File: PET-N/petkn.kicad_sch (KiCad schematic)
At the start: 83 parts, among them J1 Conn_01x20, J2 Conn_02x03_Odd_Even, J3 LINK3, J4 Conn_01x20, J5 SPACE1, J6 SPACE2, J67 LINK67, SW1 KP "=", SW10 KP "0", SW11 R SHIFT, SW12 ">", SW14 "]", SW15 "@", SW16 L SHIFT, SW17 KP "+", SW18 KP "2", SW2 KP ".", SW20 "?", SW21 ",", SW22 "N", SW23 "V", SW24 "X", SW25 KP "3", SW26 KP "1", SW27 RETURN, SW28 ";", SW29 "M", SW3 NC ($10), SW30 "B", SW31 "C", SW32 "Z", SW320 S LOCK, SW33 KP "*", SW34 KP "5", SW36 ":", SW37 "K", SW38 "H", SW39 "F", SW4 STOP, SW40 "S", SW41 KP "6", SW42 KP "4", SW44 "L", SW45 "J", SW46 "G", SW47 "D", SW48 "A", SW49 KP "/", SW5 "<", SW50 KP "8", SW52 "P", SW53 "I", SW54 "Y", SW55 "R", SW56 "W", SW57 KP "9", SW58 KP "7", SW59 U ARROW, SW6 SPACE, SW60 "O", SW61 "U", SW62 "T", SW63 "E", SW64 "Q", SW65 INS/DEL, SW66 UP/DOWN, SW67 NC ($0A), SW68 ")", SW69 "\", SW7 "[", SW70 "'", SW71 "$", SW72 QUOTE, SW73 LEFT/RIGHT, SW74 CLR/HOME, SW75 B ARROW, SW76 "(", SW77 "&", SW78 "%", SW79 "#"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

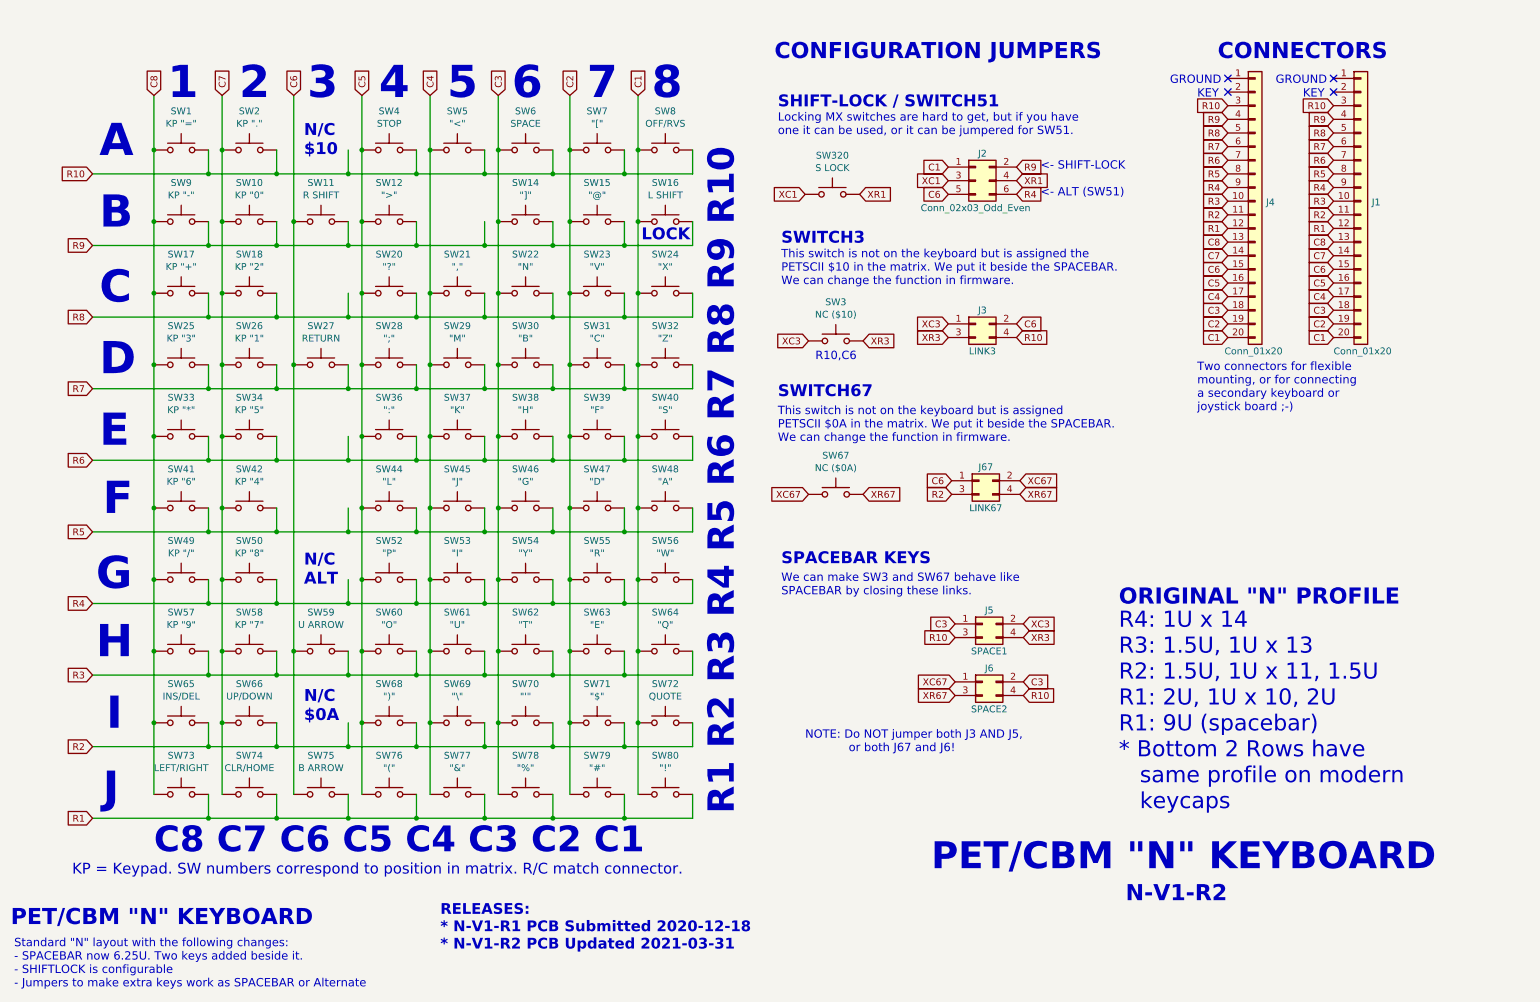
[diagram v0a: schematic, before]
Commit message: first work on adding LEDs and extended connector
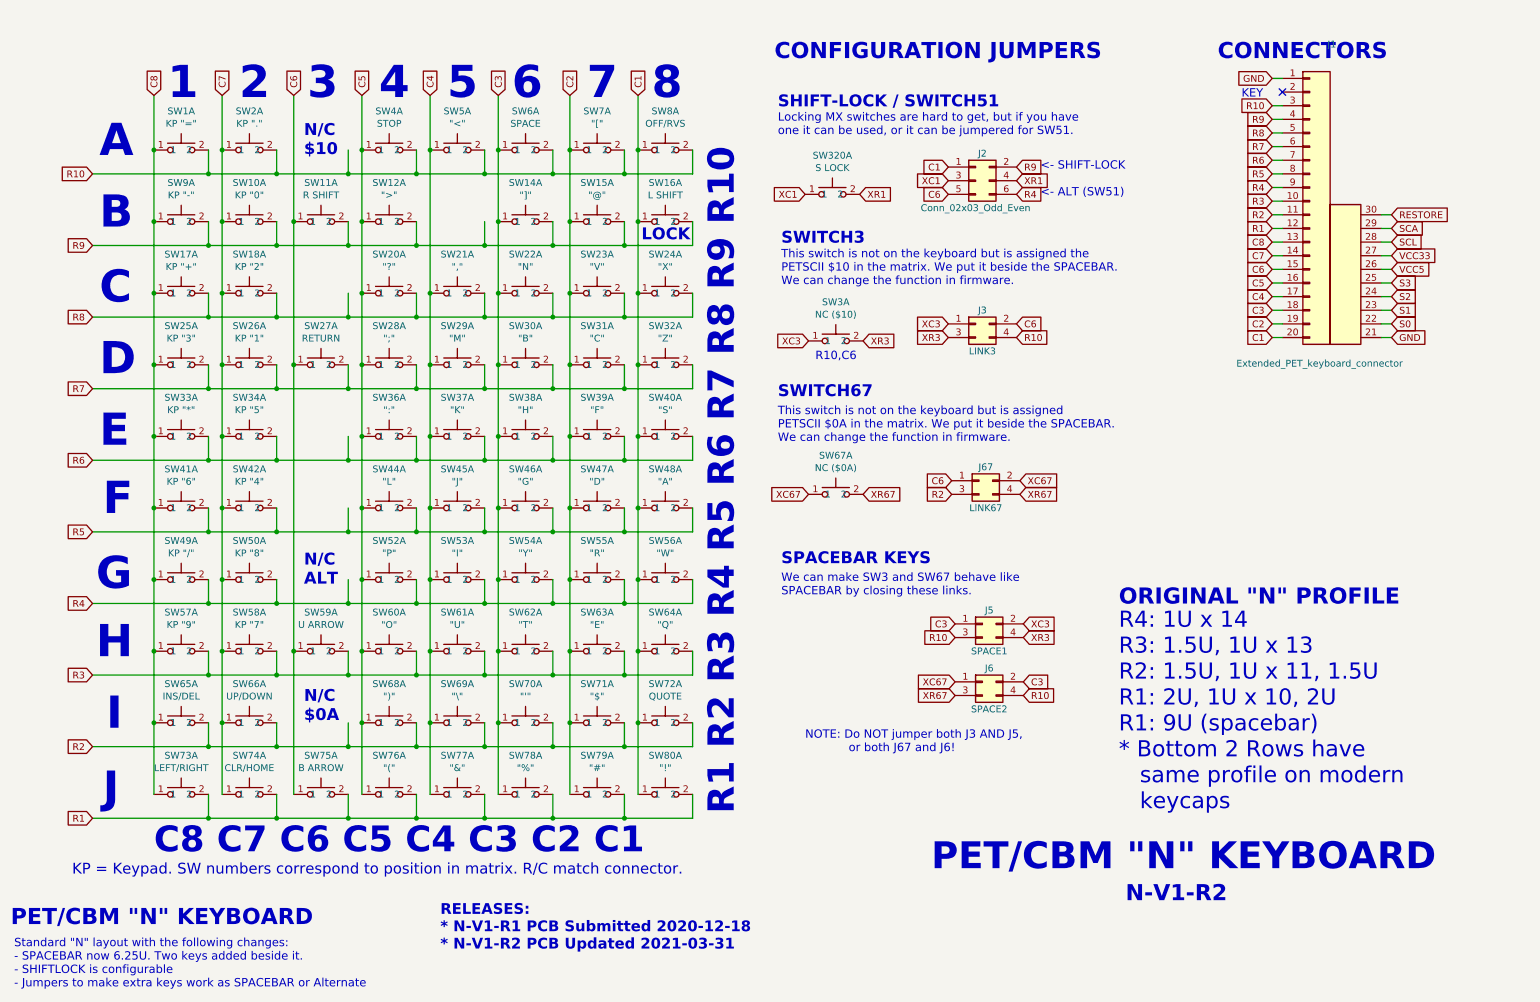
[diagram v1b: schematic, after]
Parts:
- removed J1, J4: Conn_01x20, Connector_PinHeader_2.54mm:PinHeader_1x20_P2.54mm_Vertical, symbol Connector_Generic:Conn_01x20
- added J1: Extended_PET_keyboard_connector, petkn:PET_Extended_Keyboard_Connector, symbol petkn:Extended_PET_keyboard_connector
- SW1, SW10, SW12, SW14, SW15, SW17, SW18, SW2, SW20, SW21, SW22, SW23, SW24, SW25, SW26, SW28, SW29, SW30, SW31, SW32, SW33, SW34, SW36, SW37, SW38, SW39, SW4, SW40, SW41, SW42, SW44, SW45, SW46, SW47, SW48, SW49, SW5, SW50, SW52, SW53, SW54, SW55, SW56, SW57, SW58, SW59, SW60, SW61, SW62, SW63, SW64, SW65, SW66, SW68, SW69, SW7, SW70, SW71, SW72, SW73, SW74, SW75, SW76, SW77, SW78, SW79, SW80, SW9: footprint Button_Switch_Keyboard:SW_Cherry_MX_1.00u_PCB -> petkn:SW_Cherry_MX_1.00u_PCB_with_LED; symbol Switch:SW_Push -> petkn:MX Key with LED Unit
- SW11, SW16: footprint Button_Switch_Keyboard:SW_Cherry_MX_2.00u_PCB -> petkn:SW_Cherry_MX_2.00u_PCB_with_LED; symbol Switch:SW_Push -> petkn:MX Key with LED Unit
- SW27, SW320, SW8: footprint Button_Switch_Keyboard:SW_Cherry_MX1A_1.50u_PCB -> petkn:SW_Cherry_MX_1.50u_PCB_with_LED; symbol Switch:SW_Push -> petkn:MX Key with LED Unit
- SW3: footprint Button_Switch_Keyboard:SW_Cherry_MX1A_1.25u_PCB -> petkn:SW_Cherry_MX_1.25u_PCB_with_LED; symbol Switch:SW_Push -> petkn:MX Key with LED Unit
- SW6: footprint Button_Switch_Keyboard:SW_Cherry_MX1A_6.25u_PCB -> petkn:SW_Cherry_MX_6.25u_PCB_with_LED; symbol Switch:SW_Push -> petkn:MX Key with LED Unit
- SW67: footprint Button_Switch_Keyboard:SW_Cherry_MX_1.50u_PCB -> petkn:SW_Cherry_MX_1.50u_PCB_with_LED; symbol Switch:SW_Push -> petkn:MX Key with LED Unit
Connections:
- net C1: now also J1.20 (C1)
- net C2: now also J1.19 (C2)
- net C3: now also J1.18 (C3)
- net C4: now also J1.17 (C4)
- net C5: now also J1.16 (C5)
- net C6: now also J1.15 (C6)
- net C7: now also J1.14 (C7)
- net C8: now also J1.13 (C8)
- net R1: now also J1.12 (R1)
- net R10: now also J1.3 (R10)
- net R2: now also J1.11 (R2)
- net R3: now also J1.10 (R3)
- net R4: now also J1.9 (R4)
- net R5: now also J1.8 (R5)
- net R6: now also J1.7 (R6)
- net R7: now also J1.6 (R7)
- net R8: now also J1.5 (R8)
- net R9: now also J1.4 (R9)
- new net GND: J1.1 (GND), J1.21 (GND)
- new net RESTORE: J1.30 (RESTORE)
- new net S0: J1.22 (S0)
- new net S1: J1.23 (S1)
- new net S2: J1.24 (S2)
- new net S3: J1.25 (S3)
- new net SCA: J1.29 (SCA)
- new net SCL: J1.28 (SCL)
- new net VCC33: J1.27 (VCC33)
- new net VCC5: J1.26 (VCC5)
- no-connect marks 4 -> 1
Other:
- note removed: "GROUND"
- note removed: "Two connectors for flexible mounting, or for connecting a secondary keyboard or joystick board ;-)"

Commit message: add extension page, add 4-to-10 decoder
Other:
- added sheet Extensions (extensions.kicad_sch)

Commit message: work on R3 of keyboard pcb
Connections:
- net VCC5 renamed VCC
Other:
- added sheet Driver (driver.kicad_sch)
- added sheet Row decoder (decoder.kicad_sch)
- added sheet i2c (i2c.kicad_sch)
- added sheet stick (stick.kicad_sch)
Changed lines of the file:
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@@
 		)
 	)
-	(global_label "VCC5"
+	(global_label "VCC"
 		(shape input)
 		(at 271.78 62.23 0)
@@
 		)
 		(property "Intersheetrefs" "${INTERSHEET_REFS}"
-			(at 278.9491 62.23 0)
+			(at 277.7396 62.23 0)
 			(effects
 				(font
@@
 	)
 	(sheet
+		(at 244.475 88.265)
+		(size 12.7 3.81)
+		(exclude_from_sim no)
+		(in_bom yes)
+		(on_board yes)
+		(dnp no)
+		(fields_autoplaced yes)
+		(stroke
+			(width 0.1524)
+			(type solid)
+		)
+		(fill
+			(color 0 0 0 0.0000)
+		)
+		(property "Sheetname" "i2c"
+			(at 244.475 87.5534 0)
+			(effects
+				(font
+					(size 1.27 1.27)
+				)
+				(justify left bottom)
+			)
+		)
+		(property "Sheetfile" "i2c.kicad_sch"
+			(at 244.475 92.6596 0)
+			(effects
+				(font
+					(size 1.27 1.27)
+				)
+				(justify left top)
+			)
+		)
+		(instances
+			(project "petkn"
+				(path "/a0727808-af70-4056-b2ee-ab828c2acfbd"
+					(page "3")
+				)
+			)
+		)
+	)
+	(sheet
+		(at 220.345 104.14)
+		(size 12.7 3.81)
+		(exclude_from_sim no)
+		(in_bom yes)
+		(on_board yes)
+		(dnp no)
+		(fields_autoplaced yes)
+		(stroke
+			(width 0.1524)
+			(type solid)
+		)
+		(fill
+			(color 0 0 0 0.0000)
+		)
+		(property "Sheetname" "stick"
+			(at 220.345 103.4284 0)
+			(effects
+				(font
+					(size 1.27 1.27)
+				)
+				(justify left bottom)
+			)
+		)
+		(property "Sheetfile" "stick.kicad_sch"
+			(at 220.345 108.5346 0)
+			(effects
+				(font
+					(size 1.27 1.27)
+				)
+				(justify left top)
+			)
+		)
+		(instances
+			(project "petkn"
+				(path "/a0727808-af70-4056-b2ee-ab828c2acfbd"
+					(page "6")
+				)
+			)
+		)
+	)
+	(sheet
+		(at 269.875 106.045)
+		(size 12.7 3.81)
+		(exclude_from_sim no)
+		(in_bom yes)
+		(on_board yes)
+		(dnp no)
+		(fields_autoplaced yes)
+		(stroke
+			(width 0.1524)
+			(type solid)
+		)
+		(fill
+			(color 0 0 0 0.0000)
+		)
+		(property "Sheetname" "Row decoder"
+			(at 269.875 105.3334 0)
+			(effects
+				(font
+					(size 1.27 1.27)
+				)
+				(justify left bottom)
+			)
+		)
+		(property "Sheetfile" "decoder.kicad_sch"
+			(at 269.875 110.4396 0)
+			(effects
+				(font
+					(size 1.27 1.27)
+				)
+				(justify left top)
+			)
+		)
+		(instances
+			(project "petkn"
+				(path "/a0727808-af70-4056-b2ee-ab828c2acfbd"
+					(page "5")
+				)
+			)
+		)
+	)
+	(sheet
 		(at 242.697 102.108)
 		(size 12.7 8.001)
@@
 				)
 			)
+		)
+	)
+	(sheet
+		(at 267.97 90.805)
+		(size 12.7 3.81)
+		(exclude_from_sim no)
+		(in_bom yes)
+		(on_board yes)
+		(dnp no)
+		(fields_autoplaced yes)
+		(stroke
+			(width 0.1524)
+			(type solid)
+		)
+		(fill
+			(color 0 0 0 0.0000)
+		)
+		(property "Sheetname" "Driver"
+			(at 267.97 90.0934 0)
+			(effects
+				(font
+					(size 1.27 1.27)
+				)
+				(justify left bottom)
+			)
+		)
+		(property "Sheetfile" "driver.kicad_sch"
+			(at 267.97 95.1996 0)
+			(effects
+				(font
+					(size 1.27 1.27)
+				)
+				(justify left top)
+			)
+		)
+		(instances
+			(project "petkn"
+				(path "/a0727808-af70-4056-b2ee-ab828c2acfbd"
+					(page "4")
+				)
+			)

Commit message: PET-N r3
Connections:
- net SCA renamed SDA
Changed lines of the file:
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@@
 		)
 	)
-	(global_label "SCA"
+	(global_label "SDA"
 		(shape input)
 		(at 271.78 54.61 0)

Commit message: new schematics version mainly complete
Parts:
- removed J1: Extended_PET_keyboard_connector, petkn:PET_Extended_Keyboard_Connector, symbol petkn:Extended_PET_keyboard_connector
- removed J2: Conn_02x03_Odd_Even, Connector_PinHeader_2.54mm:PinHeader_2x03_P2.54mm_Vertical, symbol Connector_Generic:Conn_02x03_Odd_Even
- removed J3: LINK3, Connector_PinHeader_2.54mm:PinHeader_2x02_P2.54mm_Vertical, symbol Connector_Generic:Conn_02x02_Odd_Even
- removed J5: SPACE1, Connector_PinHeader_2.54mm:PinHeader_2x02_P2.54mm_Vertical, symbol Connector_Generic:Conn_02x02_Odd_Even
- removed J6: SPACE2, Connector_PinHeader_2.54mm:PinHeader_2x02_P2.54mm_Vertical, symbol Connector_Generic:Conn_02x02_Odd_Even
- removed J67: LINK67, Connector_PinHeader_2.54mm:PinHeader_2x02_P2.54mm_Vertical, symbol Connector_Generic:Conn_02x02_Odd_Even
- removed SW1: KP "=", petkn:SW_Cherry_MX_1.00u_PCB_with_LED, symbol petkn:MX Key with LED Unit
- removed SW10: KP "0", petkn:SW_Cherry_MX_1.00u_PCB_with_LED, symbol petkn:MX Key with LED Unit
- removed SW11: R SHIFT, petkn:SW_Cherry_MX_2.00u_PCB_with_LED, symbol petkn:MX Key with LED Unit
- removed SW12: ">", petkn:SW_Cherry_MX_1.00u_PCB_with_LED, symbol petkn:MX Key with LED Unit
- removed SW14: "]", petkn:SW_Cherry_MX_1.00u_PCB_with_LED, symbol petkn:MX Key with LED Unit
- removed SW15: "@", petkn:SW_Cherry_MX_1.00u_PCB_with_LED, symbol petkn:MX Key with LED Unit
- removed SW16: L SHIFT, petkn:SW_Cherry_MX_2.00u_PCB_with_LED, symbol petkn:MX Key with LED Unit
- removed SW17: KP "+", petkn:SW_Cherry_MX_1.00u_PCB_with_LED, symbol petkn:MX Key with LED Unit
- removed SW18: KP "2", petkn:SW_Cherry_MX_1.00u_PCB_with_LED, symbol petkn:MX Key with LED Unit
- removed SW2: KP ".", petkn:SW_Cherry_MX_1.00u_PCB_with_LED, symbol petkn:MX Key with LED Unit
- removed SW20: "?", petkn:SW_Cherry_MX_1.00u_PCB_with_LED, symbol petkn:MX Key with LED Unit
- removed SW21: ",", petkn:SW_Cherry_MX_1.00u_PCB_with_LED, symbol petkn:MX Key with LED Unit
- removed SW22: "N", petkn:SW_Cherry_MX_1.00u_PCB_with_LED, symbol petkn:MX Key with LED Unit
- removed SW23: "V", petkn:SW_Cherry_MX_1.00u_PCB_with_LED, symbol petkn:MX Key with LED Unit
- removed SW24: "X", petkn:SW_Cherry_MX_1.00u_PCB_with_LED, symbol petkn:MX Key with LED Unit
- removed SW25: KP "3", petkn:SW_Cherry_MX_1.00u_PCB_with_LED, symbol petkn:MX Key with LED Unit
- removed SW26: KP "1", petkn:SW_Cherry_MX_1.00u_PCB_with_LED, symbol petkn:MX Key with LED Unit
- removed SW27: RETURN, petkn:SW_Cherry_MX_1.50u_PCB_with_LED, symbol petkn:MX Key with LED Unit
- removed SW28: ";", petkn:SW_Cherry_MX_1.00u_PCB_with_LED, symbol petkn:MX Key with LED Unit
- removed SW29: "M", petkn:SW_Cherry_MX_1.00u_PCB_with_LED, symbol petkn:MX Key with LED Unit
- removed SW3: NC ($10), petkn:SW_Cherry_MX_1.25u_PCB_with_LED, symbol petkn:MX Key with LED Unit
- removed SW30: "B", petkn:SW_Cherry_MX_1.00u_PCB_with_LED, symbol petkn:MX Key with LED Unit
- removed SW31: "C", petkn:SW_Cherry_MX_1.00u_PCB_with_LED, symbol petkn:MX Key with LED Unit
- removed SW32: "Z", petkn:SW_Cherry_MX_1.00u_PCB_with_LED, symbol petkn:MX Key with LED Unit
- removed SW320: S LOCK, petkn:SW_Cherry_MX_1.50u_PCB_with_LED, symbol petkn:MX Key with LED Unit
- removed SW33: KP "*", petkn:SW_Cherry_MX_1.00u_PCB_with_LED, symbol petkn:MX Key with LED Unit
- removed SW34: KP "5", petkn:SW_Cherry_MX_1.00u_PCB_with_LED, symbol petkn:MX Key with LED Unit
- removed SW36: ":", petkn:SW_Cherry_MX_1.00u_PCB_with_LED, symbol petkn:MX Key with LED Unit
- removed SW37: "K", petkn:SW_Cherry_MX_1.00u_PCB_with_LED, symbol petkn:MX Key with LED Unit
- removed SW38: "H", petkn:SW_Cherry_MX_1.00u_PCB_with_LED, symbol petkn:MX Key with LED Unit
- removed SW39: "F", petkn:SW_Cherry_MX_1.00u_PCB_with_LED, symbol petkn:MX Key with LED Unit
- removed SW4: STOP, petkn:SW_Cherry_MX_1.00u_PCB_with_LED, symbol petkn:MX Key with LED Unit
- removed SW40: "S", petkn:SW_Cherry_MX_1.00u_PCB_with_LED, symbol petkn:MX Key with LED Unit
- removed SW41: KP "6", petkn:SW_Cherry_MX_1.00u_PCB_with_LED, symbol petkn:MX Key with LED Unit
- removed SW42: KP "4", petkn:SW_Cherry_MX_1.00u_PCB_with_LED, symbol petkn:MX Key with LED Unit
- removed SW44: "L", petkn:SW_Cherry_MX_1.00u_PCB_with_LED, symbol petkn:MX Key with LED Unit
- removed SW45: "J", petkn:SW_Cherry_MX_1.00u_PCB_with_LED, symbol petkn:MX Key with LED Unit
- removed SW46: "G", petkn:SW_Cherry_MX_1.00u_PCB_with_LED, symbol petkn:MX Key with LED Unit
- removed SW47: "D", petkn:SW_Cherry_MX_1.00u_PCB_with_LED, symbol petkn:MX Key with LED Unit
- removed SW48: "A", petkn:SW_Cherry_MX_1.00u_PCB_with_LED, symbol petkn:MX Key with LED Unit
- removed SW49: KP "/", petkn:SW_Cherry_MX_1.00u_PCB_with_LED, symbol petkn:MX Key with LED Unit
- removed SW5: "<", petkn:SW_Cherry_MX_1.00u_PCB_with_LED, symbol petkn:MX Key with LED Unit
- removed SW50: KP "8", petkn:SW_Cherry_MX_1.00u_PCB_with_LED, symbol petkn:MX Key with LED Unit
- removed SW52: "P", petkn:SW_Cherry_MX_1.00u_PCB_with_LED, symbol petkn:MX Key with LED Unit
- removed SW53: "I", petkn:SW_Cherry_MX_1.00u_PCB_with_LED, symbol petkn:MX Key with LED Unit
- removed SW54: "Y", petkn:SW_Cherry_MX_1.00u_PCB_with_LED, symbol petkn:MX Key with LED Unit
- removed SW55: "R", petkn:SW_Cherry_MX_1.00u_PCB_with_LED, symbol petkn:MX Key with LED Unit
- removed SW56: "W", petkn:SW_Cherry_MX_1.00u_PCB_with_LED, symbol petkn:MX Key with LED Unit
- removed SW57: KP "9", petkn:SW_Cherry_MX_1.00u_PCB_with_LED, symbol petkn:MX Key with LED Unit
- removed SW58: KP "7", petkn:SW_Cherry_MX_1.00u_PCB_with_LED, symbol petkn:MX Key with LED Unit
- removed SW59: U ARROW, petkn:SW_Cherry_MX_1.00u_PCB_with_LED, symbol petkn:MX Key with LED Unit
- removed SW6: SPACE, petkn:SW_Cherry_MX_6.25u_PCB_with_LED, symbol petkn:MX Key with LED Unit
- removed SW60: "O", petkn:SW_Cherry_MX_1.00u_PCB_with_LED, symbol petkn:MX Key with LED Unit
- removed SW61: "U", petkn:SW_Cherry_MX_1.00u_PCB_with_LED, symbol petkn:MX Key with LED Unit
- removed SW62: "T", petkn:SW_Cherry_MX_1.00u_PCB_with_LED, symbol petkn:MX Key with LED Unit
- removed SW63: "E", petkn:SW_Cherry_MX_1.00u_PCB_with_LED, symbol petkn:MX Key with LED Unit
- removed SW64: "Q", petkn:SW_Cherry_MX_1.00u_PCB_with_LED, symbol petkn:MX Key with LED Unit
- removed SW65: INS/DEL, petkn:SW_Cherry_MX_1.00u_PCB_with_LED, symbol petkn:MX Key with LED Unit
- removed SW66: UP/DOWN, petkn:SW_Cherry_MX_1.00u_PCB_with_LED, symbol petkn:MX Key with LED Unit
- removed SW67: NC ($0A), petkn:SW_Cherry_MX_1.50u_PCB_with_LED, symbol petkn:MX Key with LED Unit
- removed SW68: ")", petkn:SW_Cherry_MX_1.00u_PCB_with_LED, symbol petkn:MX Key with LED Unit
- removed SW69: "\", petkn:SW_Cherry_MX_1.00u_PCB_with_LED, symbol petkn:MX Key with LED Unit
- removed SW7: "[", petkn:SW_Cherry_MX_1.00u_PCB_with_LED, symbol petkn:MX Key with LED Unit
- removed SW70: "'", petkn:SW_Cherry_MX_1.00u_PCB_with_LED, symbol petkn:MX Key with LED Unit
- removed SW71: "$", petkn:SW_Cherry_MX_1.00u_PCB_with_LED, symbol petkn:MX Key with LED Unit
- removed SW72: QUOTE, petkn:SW_Cherry_MX_1.00u_PCB_with_LED, symbol petkn:MX Key with LED Unit
- removed SW73: LEFT/RIGHT, petkn:SW_Cherry_MX_1.00u_PCB_with_LED, symbol petkn:MX Key with LED Unit
- removed SW74: CLR/HOME, petkn:SW_Cherry_MX_1.00u_PCB_with_LED, symbol petkn:MX Key with LED Unit
- removed SW75: B ARROW, petkn:SW_Cherry_MX_1.00u_PCB_with_LED, symbol petkn:MX Key with LED Unit
- removed SW76: "(", petkn:SW_Cherry_MX_1.00u_PCB_with_LED, symbol petkn:MX Key with LED Unit
- removed SW77: "&", petkn:SW_Cherry_MX_1.00u_PCB_with_LED, symbol petkn:MX Key with LED Unit
- removed SW78: "%", petkn:SW_Cherry_MX_1.00u_PCB_with_LED, symbol petkn:MX Key with LED Unit
- removed SW79: "#", petkn:SW_Cherry_MX_1.00u_PCB_with_LED, symbol petkn:MX Key with LED Unit
- removed SW8: OFF/RVS, petkn:SW_Cherry_MX_1.50u_PCB_with_LED, symbol petkn:MX Key with LED Unit
- removed SW80: "!", petkn:SW_Cherry_MX_1.00u_PCB_with_LED, symbol petkn:MX Key with LED Unit
- removed SW9: KP "-", petkn:SW_Cherry_MX_1.00u_PCB_with_LED, symbol petkn:MX Key with LED Unit
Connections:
- no-connect marks 1 -> 0
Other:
- removed sheet Driver
- removed sheet Extensions
- removed sheet Row decoder
- removed sheet i2c
- removed sheet stick
- added sheet keys (keys.kicad_sch)
- added sheet ledctrl (ledctrl.kicad_sch)
- added sheet leds (leds.kicad_sch)
- added sheet scanner (scanner.kicad_sch)
- note added: "Assembly options: 1. Original: No ICs Use original single row 20pin connector Solder Jumper JP1 and JP2 2. Full uPET with key scanner/mapper: All ICs Use 20pin IDC (2row) connector Requires 3.3V and 5V supply and I2C for control 3. IDC connector without mapper/leds Only use ICx (4-to-10 mapper) Use 20pin IDC (2row) connector Requires 5V power supply only"
- note removed: "1"
- note removed: "2"
- note removed: "3"
- note removed: "4"
- note removed: "5"
- note removed: "6"
- note removed: "7"
- note removed: "8"
- note removed: "<- SHIFT-LOCK <- ALT (SW51)"
- note removed: "A"
- note removed: "B"
- note removed: "C"
- note removed: "C8 C7 C6 C5 C4 C3 C2 C1"
- note removed: "CONFIGURATION JUMPERS"
- note removed: "CONNECTORS"
- note removed: "D"
- note removed: "E"
- note removed: "F"
- note removed: "G"
- note removed: "H"
- note removed: "I"
- note removed: "J"
- note removed: "KEY"
- note removed: "KP = Keypad. SW numbers correspond to position in matrix. R/C match connector."
- note removed: "LOCK"
- note removed: "Locking MX switches are hard to get, but if you have one it can be used, or it can be jumpered for SW51."
- note removed: "N-V1-R2"
- note removed: "N/C $0A"
- note removed: "N/C $10"
- note removed: "N/C ALT"
- note removed: "NOTE: Do NOT jumper both J3 AND J5, or both J67 and J6!"
- note removed: "ORIGINAL "N" PROFILE"
- note removed: "PET/CBM "N" KEYBOARD"
- note removed: "R1 R2 R3 R4 R5 R6 R7 R8 R9 R10"
- note removed: "R10,C6"
- note removed: "R4: 1U x 14 R3: 1.5U, 1U x 13 R2: 1.5U, 1U x 11, 1.5U R1: 2U, 1U x 10, 2U R1: 9U (spacebar) * Bottom 2 Rows have same profile on modern keycaps"
- note removed: "RELEASES: * N-V1-R1 PCB Submitted 2020-12-18 * N-V1-R2 PCB Updated 2021-03-31"
- note removed: "SHIFT-LOCK / SWITCH51"
- note removed: "SPACEBAR KEYS"
- note removed: "SWITCH3"
- note removed: "SWITCH67"
- note removed: "Standard "N" layout with the following changes: - SPACEBAR now 6.25U. Two keys added beside it. - SHIFTLOCK is configurable - Jumpers to make extra keys work as SPACEBAR or Alternate"
- note removed: "This switch is not on the keyboard but is assigned PETSCII $0A in the matrix. We put it beside the SPACEBAR. We can change the function in firmware."
- note removed: "This switch is not on the keyboard but is assigned the PETSCII $10 in the matrix. We put it beside the SPACEBAR. We can change the function in firmware."
- note removed: "We can make SW3 and SW67 behave like SPACEBAR by closing these links."

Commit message: more layout work
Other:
- note added: "Assembly options: 1. Original: No ICs Use original single row 20pin connector Solder Jumper JP1 and JP2 2. Full uPET with key scanner/mapper: All ICs Use 20pin IDC (2row) connector Requires 3.3V and 5V supply and I2C for control 3. IDC connector without mapper/leds Only use U7 (4-to-10 mapper) Use 20pin IDC (2row) connector Requires 5V power supply only"
- note removed: "Assembly options: 1. Original: No ICs Use original single row 20pin connector Solder Jumper JP1 and JP2 2. Full uPET with key scanner/mapper: All ICs Use 20pin IDC (2row) connector Requires 3.3V and 5V supply and I2C for control 3. IDC connector without mapper/leds Only use ICx (4-to-10 mapper) Use 20pin IDC (2row) connector Requires 5V power supply only"
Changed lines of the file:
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@@
 		(company "Steve J. Gray")
 	)
-	(text "Assembly options:\n1. Original:\n   No ICs\n   Use original single row 20pin connector\n   Solder Jumper JP1 and JP2\n2. Full uPET with key scanner/mapper:\n   All ICs\n   Use 20pin IDC (2row) connector\n   Requires 3.3V and 5V supply and I2C for control\n3. IDC connector without mapper/leds\n   Only use ICx (4-to-10 mapper)\n   Use 20pin IDC (2row) connector\n   Requires 5V power supply only"
+	(text "Assembly options:\n1. Original:\n   No ICs\n   Use original single row 20pin connector\n   Solder Jumper JP1 and JP2\n2. Full uPET with key scanner/mapper:\n   All ICs\n   Use 20pin IDC (2row) connector\n   Requires 3.3V and 5V supply and I2C for control\n3. IDC connector without mapper/leds\n   Only use U7 (4-to-10 mapper)\n   Use 20pin IDC (2row) connector\n   Requires 5V power supply only"
 		(exclude_from_sim no)
 		(at 43.942 98.806 0)
